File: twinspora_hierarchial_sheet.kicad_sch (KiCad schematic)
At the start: 90 parts, among them J1 TYPE-C-31-M-12, J10 XY-SH1_0-4A61, J12 XY-XH2_54-5A21, J13 Conn_01x02, J2 XT30U-M, J3 XT60PW-M, J4 Conn_01x02, J5 XY-XH2_54-2A21, J6 XY-XH2_54-2A21, J7 Conn_01x02, J8 XY-SH1_0-6A51, J9 XY-SH1_0-6A51, Q1 AO3401A, SW2 TS1187A26020, SW3 TS1187A26020, U1 STM32G473RBTx, U4 XC6206P332MR, U5 CA-IF1044VD-Q1, U8 MT6701QT, U9 MT6701QT, X1 X322512MSB4SI

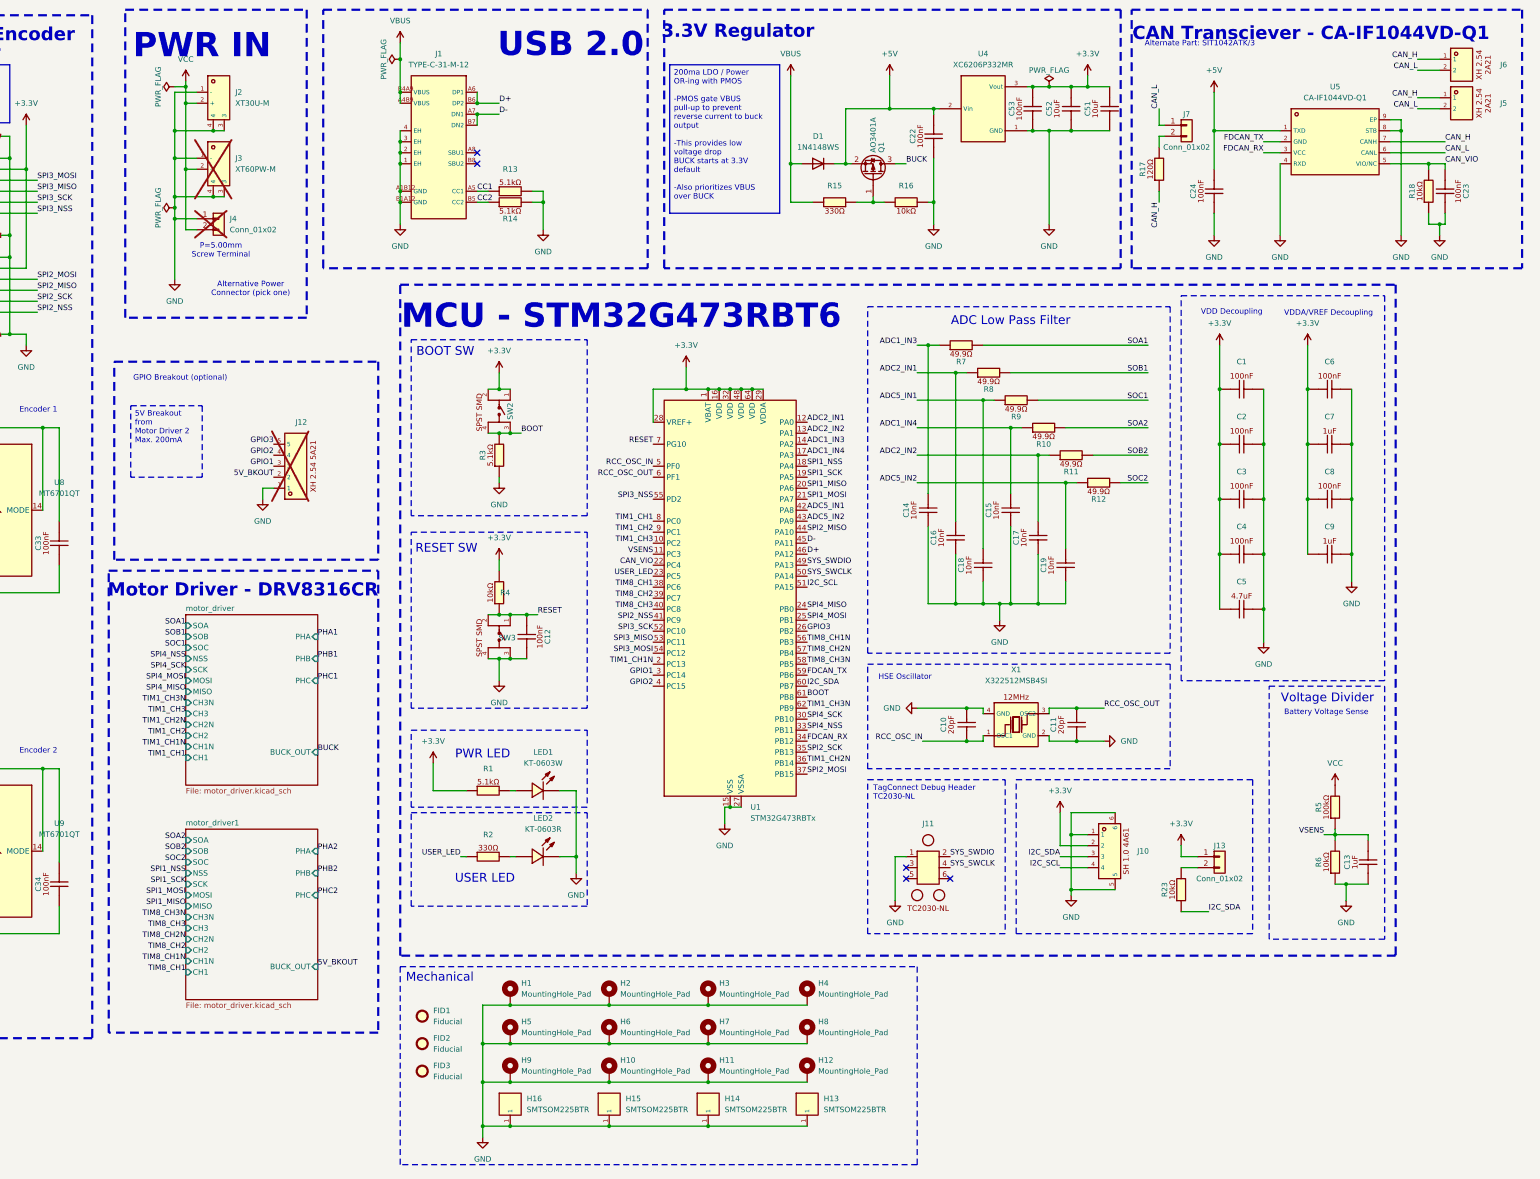
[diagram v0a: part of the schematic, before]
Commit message: added smt nut
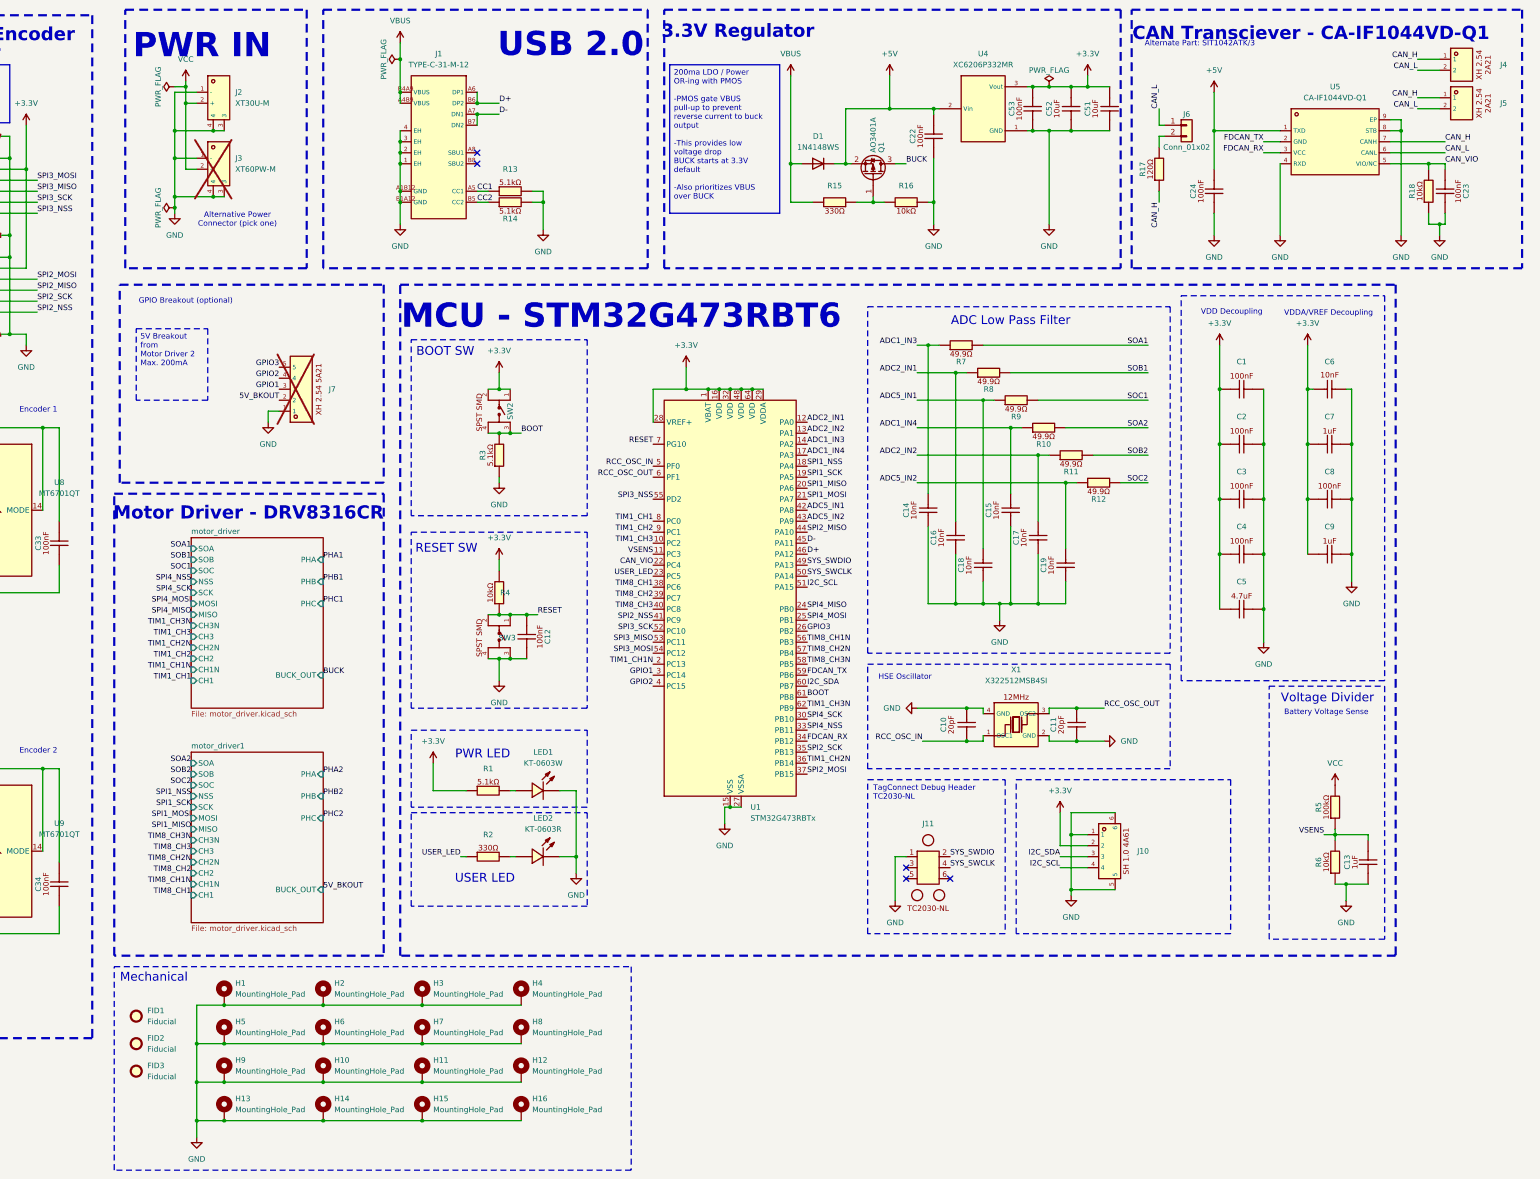
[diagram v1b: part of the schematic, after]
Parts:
- removed C6: CL05B104KB54PNC, Basic_Capacitors_Resistors:C0402, symbol Basic_Capacitors_Resistors:CL05B104KB54PNC
- removed H13, H14, H15, H16: SMTSOM225BTR, footprints/Mechanical:SMD_BD5.6-D3.6, symbol Mechanical:SMTSOM225BTR
- removed J13: Conn_01x02, Connector_PinSocket_2.54mm:PinSocket_1x02_P2.54mm_Vertical, symbol Connector_Generic:Conn_01x02
- removed J4: Conn_01x02, Connector_Phoenix_MSTB:PhoenixContact_MSTBA_2,5_2-G_1x02_P5.00mm_Horizontal, symbol Connector_Generic:Conn_01x02
- removed R23: 0402WGF1002TCE, Basic_Capacitors_Resistors:R0402, symbol Basic_Capacitors_Resistors:0402WGF1002TCE
- added C6: CL05B103KB5NNNC, Basic_Capacitors_Resistors:C0402, symbol Basic_Capacitors_Resistors:CL05B103KB5NNNC
- added H13, H14, H15, H16: MountingHole_Pad, symbol Mechanical:MountingHole_Pad
- renumbered J6 to J4, J7 to J6, J12 to J7
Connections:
- net +3.3V: now also C6.1
- net GND: now also C6.2, H13.1, H14.1, H15.1, H16.1
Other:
- note removed: "P=5.00mm Screw Terminal"
- moved on the sheet: FID1, FID2, FID3, H1, H10, H11, H12, H2, H3, H4, H5, H6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
